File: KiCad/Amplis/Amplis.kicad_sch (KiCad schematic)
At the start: 15 parts, among them U1 LTC6090, U2 LTC6090

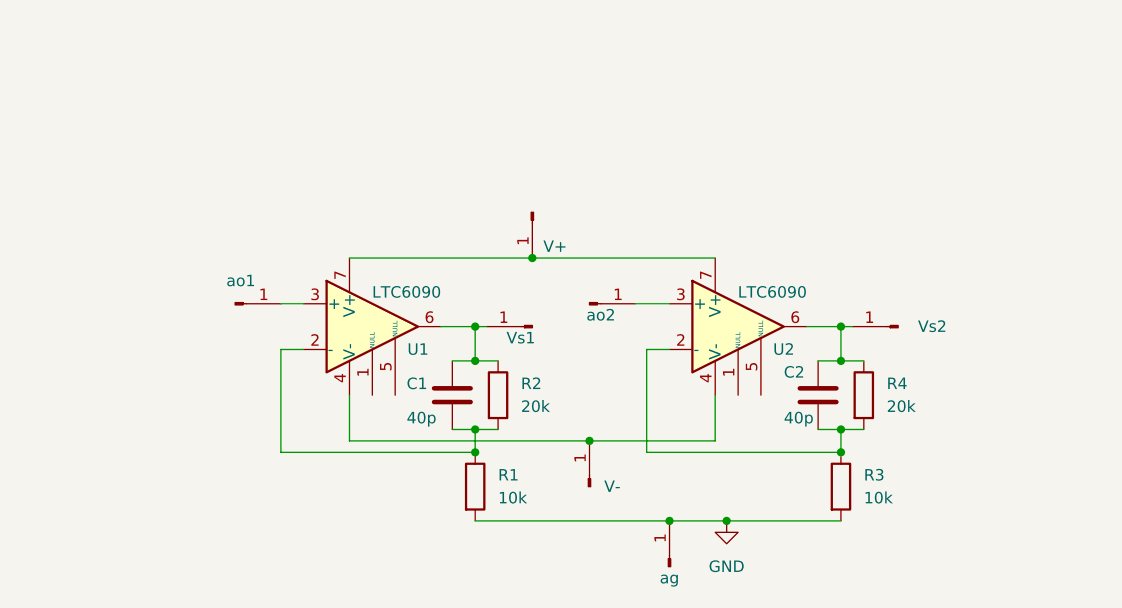
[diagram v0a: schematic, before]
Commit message: Better schematics + 3D models + New images
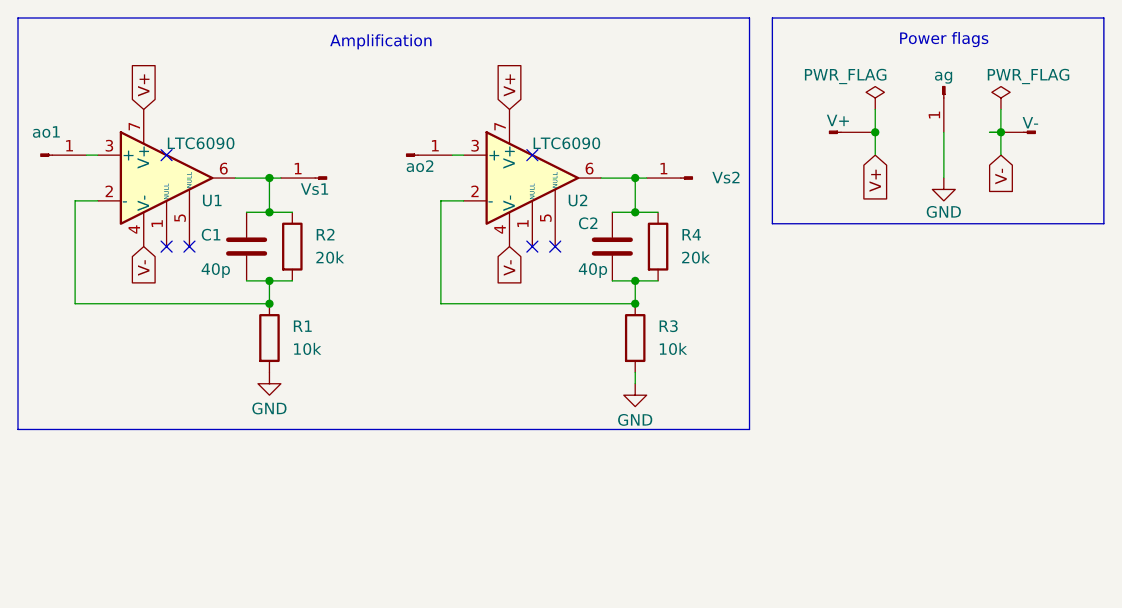
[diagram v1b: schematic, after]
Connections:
- net V-: now reaches U1.4 (V-), U2.4 (V-), V-.1 (Pin_1)
- net V+: now reaches U1.7 (V+), U2.7 (V+), V+.1 (Pin_1)
- no-connect marks 0 -> 6
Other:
- note added: "Amplification"
- note added: "Power flags"
- moved on the sheet: C1, C2, R1, R2, R3, R4, U1, U2, Vs1, Vs2, ag, ao1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
